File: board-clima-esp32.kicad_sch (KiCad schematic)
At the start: 54 parts, among them IC1 ESP32-S3-WROOM-1-N4, J1 Conn_01x06_Pin, J2 Screw_Terminal_01x03, J3 Conn_01x04_Pin, J5 Conn_01x05_Pin, J6 USB_C_Receptacle, Q1 AO3400A, Q2 AO3401A, Q3 AO3400A, SW1 RESET, SW2 BOOT, U1 AMS1117-3.3, U3 PC817, U4 PC817

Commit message: rev2 routing
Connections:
- net R_COM: now also U2.13 (CM2); no longer U2.4 (CM1)
- net R_NC: now also U2.11 (NC2); no longer U2.6 (NC1)
- net R_NO: now also U2.9 (NO2); no longer U2.8 (NO1)
- net at D1.2 (A), Q1.3 (D): now also U2.16 (S2); no longer U2.1 (S1)
- net at D2.1 (K), R8.2: now also U2.2 (R1); no longer U2.15 (R2)
- net at D1.1 (K), R4.2: now also U2.1 (S1); no longer U2.16 (S2)
- net at D2.2 (A), Q3.3 (D): now also U2.15 (R2); no longer U2.2 (R1)
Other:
- moved on the sheet: U2
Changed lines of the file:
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@@
   (junction (at 240.03 72.39) (diameter 0) (color 0 0 0 0)
   )
+  (junction (at 198.12 135.89) (diameter 0) (color 0 0 0 0)
+  )
+  (junction (at 102.87 26.67) (diameter 0) (color 0 0 0 0)
+  )
+  (junction (at 209.55 120.65) (diameter 0) (color 0 0 0 0)
+  )
+  (junction (at 300.99 78.74) (diameter 0) (color 0 0 0 0)
+  )
+  (junction (at 93.98 26.67) (diameter 0) (color 0 0 0 0)
+  )
+  (junction (at 240.03 69.85) (diameter 0) (color 0 0 0 0)
+  )
+  (junction (at 182.88 34.29) (diameter 0) (color 0 0 0 0)
+  )
+  (junction (at 182.88 85.09) (diameter 0) (color 0 0 0 0)
+  )
+  (junction (at 115.57 39.37) (diameter 0) (color 0 0 0 0)
+  )
+  (junction (at 186.69 99.06) (diameter 0) (color 0 0 0 0)
+  )
   (junction (at 92.71 152.4) (diameter 0) (color 0 0 0 0)
-  )
-  (junction (at 198.12 135.89) (diameter 0) (color 0 0 0 0)
-  )
-  (junction (at 102.87 26.67) (diameter 0) (color 0 0 0 0)
-  )
-  (junction (at 209.55 120.65) (diameter 0) (color 0 0 0 0)
-  )
-  (junction (at 300.99 78.74) (diameter 0) (color 0 0 0 0)
-  )
-  (junction (at 93.98 26.67) (diameter 0) (color 0 0 0 0)
-  )
-  (junction (at 240.03 69.85) (diameter 0) (color 0 0 0 0)
-  )
-  (junction (at 182.88 34.29) (diameter 0) (color 0 0 0 0)
-  )
-  (junction (at 182.88 85.09) (diameter 0) (color 0 0 0 0)
-  )
-  (junction (at 115.57 39.37) (diameter 0) (color 0 0 0 0)
-  )
-  (junction (at 186.69 99.06) (diameter 0) (color 0 0 0 0)
   )
   (junction (at 198.12 146.05) (diameter 0) (color 0 0 0 0)
@@
   (no_connect (at 240.03 52.07))
   (no_connect (at 45.72 64.77))
-  (no_connect (at 101.6 132.08))
   (no_connect (at 45.72 59.69))
   (no_connect (at 240.03 46.99))
@@
   (no_connect (at 45.72 57.15))
   (no_connect (at 207.01 44.45))
+  (no_connect (at 101.6 133.35))
   (no_connect (at 45.72 49.53))
   (no_connect (at 45.72 72.39))
@@
   (no_connect (at 45.72 82.55))
   (no_connect (at 240.03 34.29))
-  (no_connect (at 99.06 132.08))
   (no_connect (at 240.03 44.45))
   (no_connect (at 45.72 67.31))
@@
   (no_connect (at 45.72 74.93))
   (no_connect (at 207.01 67.31))
-  (no_connect (at 96.52 132.08))
+  (no_connect (at 99.06 133.35))
   (no_connect (at 207.01 49.53))
   (no_connect (at 207.01 54.61))
@@
   (no_connect (at 207.01 36.83))
   (no_connect (at 45.72 52.07))
+  (no_connect (at 96.52 133.35))
   (no_connect (at 207.01 57.15))
   (no_connect (at 240.03 36.83))
@@
     (stroke (width 0) (type default))
   )
+  (wire (pts (xy 92.71 148.59) (xy 92.71 152.4))
+    (stroke (width 0) (type default))
+  )
   (wire (pts (xy 397.51 77.47) (xy 403.86 77.47))
     (stroke (width 0) (type default))
@@
     (stroke (width 0) (type default))
   )
+  (wire (pts (xy 90.17 123.19) (xy 90.17 133.35))
+    (stroke (width 0) (type default))
+  )
   (wire (pts (xy 189.23 99.06) (xy 186.69 99.06))
     (stroke (width 0) (type default))
@@
     (stroke (width 0) (type default))
   )
-  (wire (pts (xy 90.17 147.32) (xy 90.17 149.86))
-    (stroke (width 0) (type default))
-  )
   (wire (pts (xy 45.72 24.13) (xy 53.34 24.13))
     (stroke (width 0) (type default))
@@
     (stroke (width 0) (type default))
   )
-  (wire (pts (xy 90.17 123.19) (xy 90.17 132.08))
-    (stroke (width 0) (type default))
-  )
   (wire (pts (xy 160.02 34.29) (xy 168.91 34.29))
     (stroke (width 0) (type default))
@@
     (stroke (width 0) (type default))
   )
+  (wire (pts (xy 92.71 128.27) (xy 92.71 133.35))
+    (stroke (width 0) (type default))
+  )
   (wire (pts (xy 300.99 73.66) (xy 300.99 78.74))
     (stroke (width 0) (type default))
@@
     (stroke (width 0) (type default))
   )
-  (wire (pts (xy 96.52 147.32) (xy 96.52 154.94))
-    (stroke (width 0) (type default))
-  )
   (wire (pts (xy 195.58 59.69) (xy 207.01 59.69))
     (stroke (width 0) (type default))
@@
     (stroke (width 0) (type default))
   )
+  (wire (pts (xy 99.06 148.59) (xy 99.06 152.4))
+    (stroke (width 0) (type default))
+  )
   (wire (pts (xy 209.55 128.27) (xy 209.55 130.81))
     (stroke (width 0) (type default))
@@
     (stroke (width 0) (type default))
   )
-  (wire (pts (xy 92.71 147.32) (xy 92.71 152.4))
-    (stroke (width 0) (type default))
-  )
   (wire (pts (xy 102.87 36.83) (xy 102.87 39.37))
     (stroke (width 0) (type default))
@@
     (stroke (width 0) (type default))
   )
+  (wire (pts (xy 96.52 148.59) (xy 96.52 154.94))
+    (stroke (width 0) (type default))
+  )
   (wire (pts (xy 173.99 128.27) (xy 173.99 130.81))
     (stroke (width 0) (type default))
@@
     (stroke (width 0) (type default))
   )
-  (wire (pts (xy 99.06 147.32) (xy 99.06 152.4))
-    (stroke (width 0) (type default))
-  )
   (wire (pts (xy 128.27 26.67) (xy 134.62 26.67))
     (stroke (width 0) (type default))
@@
     (stroke (width 0) (type default))
   )
+  (wire (pts (xy 90.17 148.59) (xy 90.17 149.86))
+    (stroke (width 0) (type default))
+  )
   (wire (pts (xy 166.37 140.97) (xy 173.99 140.97))
     (stroke (width 0) (type default))
   )
-  (wire (pts (xy 101.6 147.32) (xy 101.6 149.86))
-    (stroke (width 0) (type default))
-  )
   (wire (pts (xy 96.52 154.94) (xy 107.95 154.94))
     (stroke (width 0) (type default))
   )
+  (wire (pts (xy 101.6 148.59) (xy 101.6 149.86))
+    (stroke (width 0) (type default))
+  )
   (wire (pts (xy 198.12 133.35) (xy 198.12 135.89))
     (stroke (width 0) (type default))
@@
   )
   (wire (pts (xy 299.72 76.2) (xy 302.26 76.2))
-    (stroke (width 0) (type default))
-  )
-  (wire (pts (xy 92.71 128.27) (xy 92.71 132.08))
     (stroke (width 0) (type default))
   )
@@
     )
   )
-  (symbol (lib_id "HFD2:HFD2/00X-M-L2") (at 88.9 134.62 0) (unit 1)
-    (in_bom yes) (on_board yes) (dnp no) (fields_autoplaced)
-    (property "Reference" "U2" (at 104.14 139.7 0)
+  (symbol (lib_id "HFD2:HFD2/00X-M-L2") (at 88.9 146.05 0) (mirror x) (unit 1)
+    (in_bom yes) (on_board yes) (dnp no)
+    (property "Reference" "U2" (at 104.14 140.97 0)
       (effects (font (size 1.27 1.27)) (justify left))
     )
-    (property "Value" "~" (at 88.9 134.62 0)
+    (property "Value" "~" (at 88.9 146.05 0)
       (effects (font (size 1.27 1.27)))
     )
-    (property "Footprint" "HFD2:HFD2-00X-M-L2" (at 96.52 120.65 0)
-      (effects (font (size 1.27 1.27)) hide)
-    )
-    (property "Datasheet" "https://pdf1.alldatasheet.com/datasheet-pdf/download/660910/HONGFA/HFD2SLASH005-S-L2-D.html" (at 93.98 123.19 0)
-      (effects (font (size 1.27 1.27)) hide)
-    )
+    (property "Footprint" "HFD2:HFD2-00X-M-L2" (at 96.52 160.02 0)
+      (effects (font (size 1.27 1.27)) hide)
+    )
+    (property "Datasheet" "https://pdf1.alldatasheet.com/datasheet-pdf/download/660910/HONGFA/HFD2SLASH005-S-L2-D.html" (at 93.98 157.48 0)
+      (effects (font (size 1.27 1.27)) hide)
+    )

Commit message: silkscreen
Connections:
- net GND: now also J5.4 (Pin_4); no longer J5.1 (Pin_1)
- net GPIO3: now also J5.1 (Pin_1); no longer J5.4 (Pin_4)
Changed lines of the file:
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@@
+    (effects (font (size 1.27 1.27)) (justify left bottom))
+  )
+  (label "GPIO3" (at 374.65 36.83 0) (fields_autoplaced)
     (effects (font (size 1.27 1.27)) (justify left bottom))
   )
@@
     (effects (font (size 1.27 1.27)) (justify left bottom))
   )
+  (label "GPIO1" (at 374.65 31.75 0) (fields_autoplaced)
+    (effects (font (size 1.27 1.27)) (justify left bottom))
+  )
   (label "SCK" (at 173.99 85.09 0) (fields_autoplaced)
     (effects (font (size 1.27 1.27)) (justify left bottom))
@@
     (effects (font (size 1.27 1.27)) (justify left bottom))
   )
+  (label "GPIO2" (at 374.65 34.29 0) (fields_autoplaced)
+    (effects (font (size 1.27 1.27)) (justify left bottom))
+  )
   (label "R_NO" (at 386.08 59.69 0) (fields_autoplaced)
     (effects (font (size 1.27 1.27)) (justify left bottom))
@@
     (effects (font (size 1.27 1.27)) (justify left bottom))
   )
-  (label "GPIO1" (at 374.65 31.75 0) (fields_autoplaced)
-    (effects (font (size 1.27 1.27)) (justify left bottom))
-  )
   (label "BOILER_1" (at 33.02 158.75 0) (fields_autoplaced)
     (effects (font (size 1.27 1.27)) (justify left bottom))
@@
     (effects (font (size 1.27 1.27)) (justify left bottom))
   )
-  (label "GPIO3" (at 374.65 29.21 0) (fields_autoplaced)
-    (effects (font (size 1.27 1.27)) (justify left bottom))
-  )
   (label "R_NO" (at 175.26 130.81 0) (fields_autoplaced)
     (effects (font (size 1.27 1.27)) (justify left bottom))
@@
     (effects (font (size 1.27 1.27)) (justify left bottom))
   )
-  (label "GPIO2" (at 374.65 34.29 0) (fields_autoplaced)
-    (effects (font (size 1.27 1.27)) (justify left bottom))
-  )
   (label "BOILER_1" (at 173.99 72.39 0) (fields_autoplaced)
     (effects (font (size 1.27 1.27)) (justify left bottom))
@@
   (label "BOOT" (at 245.745 31.75 0) (fields_autoplaced)
     (effects (font (size 1.27 1.27)) (justify left bottom))
-  )
-  (symbol (lib_id "power:GND") (at 374.65 36.83 0) (unit 1)
-    (in_bom yes) (on_board yes) (dnp no) (fields_autoplaced)
-    (property "Reference" "#PWR034" (at 374.65 43.18 0)
-      (effects (font (size 1.27 1.27)) hide)
-    )
-    (property "Value" "GND" (at 374.65 41.91 0)
-      (effects (font (size 1.27 1.27)))
-    )
-    (property "Footprint" "" (at 374.65 36.83 0)
-      (effects (font (size 1.27 1.27)) hide)
-    )
-    (property "Datasheet" "" (at 374.65 36.83 0)
-      (effects (font (size 1.27 1.27)) hide)
-    )
-    (pin "1")
-    (instances
-      (project "board-clima-esp32"
-        (path "/ec184202-d4fa-4f1f-9fe7-c32d14dd4c20"
-          (reference "#PWR034") (unit 1)
-        )
-      )
-    )
   )
   (symbol (lib_id "power:+3.3V") (at 335.28 26.67 0) (unit 1)
@@
         )
       )
+    )
+  )
+  (symbol (lib_id "power:GND") (at 374.65 29.21 270) (unit 1)
+    (in_bom yes) (on_board yes) (dnp no) (fields_autoplaced)
+    (property "Reference" "#PWR021" (at 368.3 29.21 0)
+      (effects (font (size 1.27 1.27)) hide)
+    )
+    (property "Value" "GND" (at 370.84 29.21 90)
+      (effects (font (size 1.27 1.27)) (justify right))
+    )
+    (property "Footprint" "" (at 374.65 29.21 0)
+      (effects (font (size 1.27 1.27)) hide)
+    )
+    (property "Datasheet" "" (at 374.65 29.21 0)
+      (effects (font (size 1.27 1.27)) hide)
+    )
+    (pin "1")
+    (instances
+      (project "board-clima-esp32"
+        (path "/ec184202-d4fa-4f1f-9fe7-c32d14dd4c20"
+          (reference "#PWR021") (unit 1)
+        )
+      )

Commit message: drc passes
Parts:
- added D11: LED, LED_SMD:LED_0805_2012Metric, symbol Device:LED
- added R18: 220, Resistor_SMD:R_0805_2012Metric, symbol Device:R
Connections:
- net GND: now also R18.2
- net GPIO3: now also D11.2 (A)
- new net: D11.1 (K), R18.1
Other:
- note added: "USER LED"

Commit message: silkscreen
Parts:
- D10, D8, D9: footprint Diode_SMD:D_SOD-323 -> Diode_SMD:D_SOD-123
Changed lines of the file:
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@@
       (effects (font (size 1.27 1.27)) (justify left))
     )
-    (property "Footprint" "Diode_SMD:D_SOD-323" (at 222.25 134.62 0)
+    (property "Footprint" "Diode_SMD:D_SOD-123" (at 222.25 134.62 0)
       (effects (font (size 1.27 1.27)) hide)
     )
@@
       (effects (font (size 1.27 1.27)) (justify left))
     )
-    (property "Footprint" "Diode_SMD:D_SOD-323" (at 209.55 134.62 0)
+    (property "Footprint" "Diode_SMD:D_SOD-123" (at 209.55 134.62 0)
       (effects (font (size 1.27 1.27)) hide)
     )
@@
       (effects (font (size 1.27 1.27)) (justify left))
     )
-    (property "Footprint" "Diode_SMD:D_SOD-323" (at 193.04 144.78 0)
-      (effects (font (size 1.27 1.27)) hide)
-    )
+    (property "Footprint" "Diode_SMD:D_SOD-123" (at 193.04 144.78 0)
+      (effects (font (size 1.27 1.27)) hide)
+    )

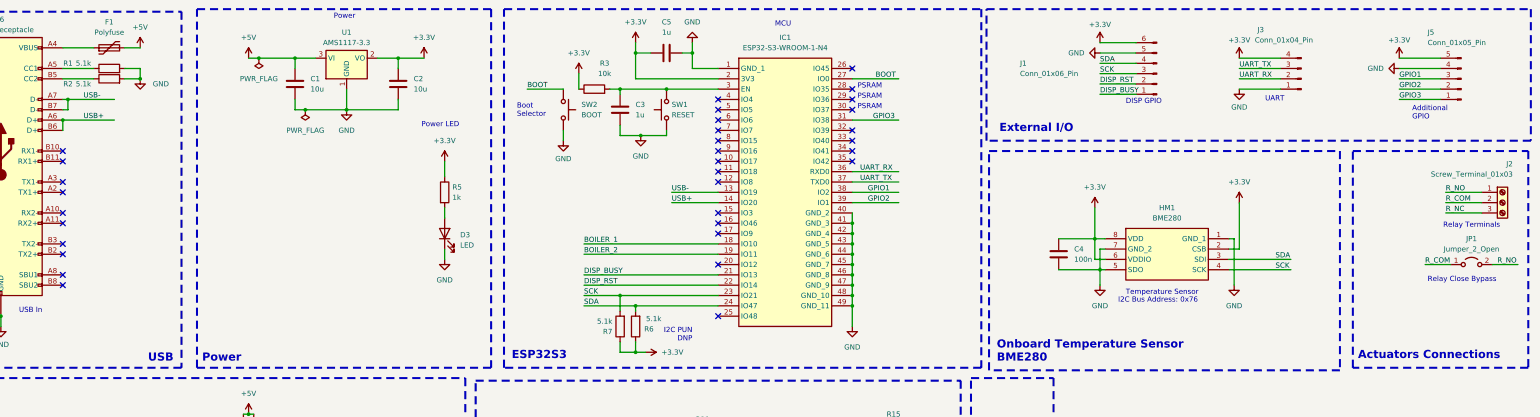
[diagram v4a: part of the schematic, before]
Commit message: new PWR connector, front copper pour
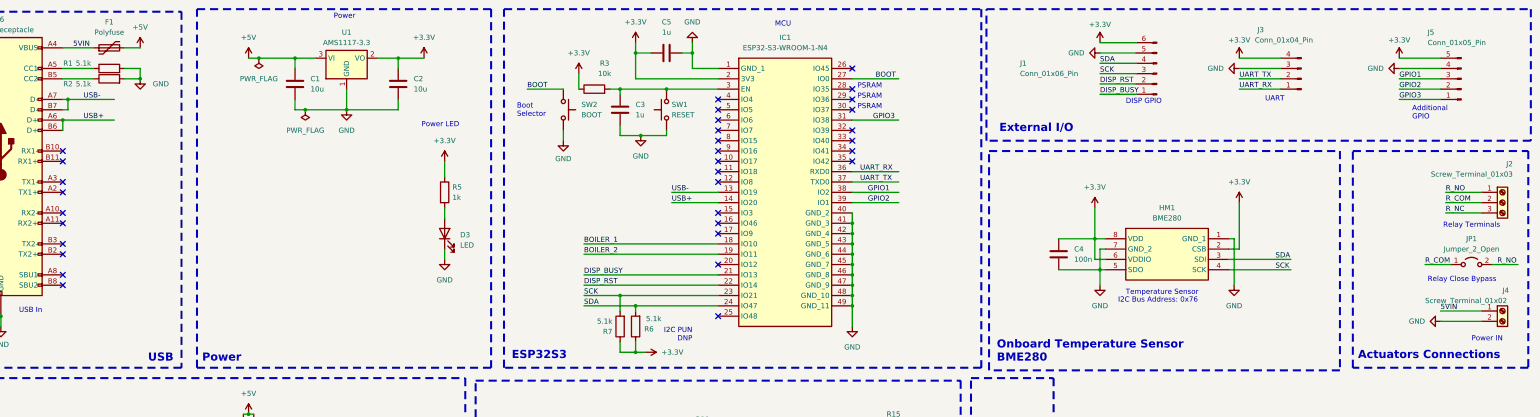
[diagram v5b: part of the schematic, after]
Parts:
- added J4: Screw_Terminal_01x02, XYEK500-5.08-3P:XYEK500-5.08-2P, symbol Connector:Screw_Terminal_01x02
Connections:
- net GND: now also J3.3 (Pin_3), J4.2 (Pin_2); no longer J3.1 (Pin_1)
- net UART_RX: now also J3.1 (Pin_1); no longer J3.2 (Pin_2)
- net UART_TX: now also J3.2 (Pin_2); no longer J3.3 (Pin_3)
- net 5VIN: now reaches F1.1, J6.A4 (VBUS), J6.A9 (VBUS), J6.B4 (VBUS), J6.B9 (VBUS)
- net 5VIN: now also J4.1 (Pin_1)
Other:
- note added: "Power IN"
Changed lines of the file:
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@@
+    (stroke (width 0) (type default))
+  )
+  (wire (pts (xy 384.81 91.44) (xy 394.97 91.44))
     (stroke (width 0) (type default))
   )
@@
   )
   (wire (pts (xy 245.11 146.05) (xy 248.92 146.05))
+    (stroke (width 0) (type default))
+  )
+  (wire (pts (xy 384.81 88.9) (xy 394.97 88.9))
     (stroke (width 0) (type default))
   )
@@
     (effects (font (size 1.27 1.27) (color 255 0 0 1)) (justify left bottom))
   )
+  (text "Power IN" (at 392.43 96.52 0)
+    (effects (font (size 1.27 1.27)) (justify left bottom))
+  )
   (text "UART" (at 341.63 37.465 0)
     (effects (font (size 1.27 1.27)) (justify left bottom))
@@
     (effects (font (size 1.27 1.27)) (justify left bottom))
   )
+  (label "5VIN" (at 48.26 24.13 0) (fields_autoplaced)
+    (effects (font (size 1.27 1.27)) (justify left bottom))
+  )
   (label "GPIO1" (at 374.65 31.75 0) (fields_autoplaced)
     (effects (font (size 1.27 1.27)) (justify left bottom))
@@
     (effects (font (size 1.27 1.27)) (justify left bottom))
   )
-  (label "UART_TX" (at 335.28 29.21 0) (fields_autoplaced)
+  (label "UART_TX" (at 335.28 31.75 0) (fields_autoplaced)
     (effects (font (size 1.27 1.27)) (justify left bottom))
   )
@@
     (effects (font (size 1.27 1.27)) (justify left bottom))
   )
-  (label "UART_RX" (at 335.28 31.75 0) (fields_autoplaced)
+  (label "UART_RX" (at 335.28 34.29 0) (fields_autoplaced)
     (effects (font (size 1.27 1.27)) (justify left bottom))
   )
@@
   )
   (label "R_NO" (at 398.78 77.47 0) (fields_autoplaced)
+    (effects (font (size 1.27 1.27)) (justify left bottom))
+  )
+  (label "5VIN" (at 384.81 88.9 0) (fields_autoplaced)
     (effects (font (size 1.27 1.27)) (justify left bottom))
   )
@@
     )
   )
-  (symbol (lib_id "power:GND") (at 335.28 34.29 0) (unit 1)
-    (in_bom yes) (on_board yes) (dnp no) (fields_autoplaced)
-    (property "Reference" "#PWR019" (at 335.28 40.64 0)
-      (effects (font (size 1.27 1.27)) hide)
-    )
-    (property "Value" "GND" (at 335.28 38.735 0)
-      (effects (font (size 1.27 1.27)))
-    )
-    (property "Footprint" "" (at 335.28 34.29 0)
-      (effects (font (size 1.27 1.27)) hide)
-    )
-    (property "Datasheet" "" (at 335.28 34.29 0)
-      (effects (font (size 1.27 1.27)) hide)
-    )
-    (pin "1")
-    (instances
-      (project "board-clima-esp32"
-        (path "/ec184202-d4fa-4f1f-9fe7-c32d14dd4c20"
-          (reference "#PWR019") (unit 1)
+  (symbol (lib_id "power:GND") (at 384.81 91.44 270) (unit 1)
+    (in_bom yes) (on_board yes) (dnp no) (fields_autoplaced)
+    (property "Reference" "#PWR035" (at 378.46 91.44 0)
+      (effects (font (size 1.27 1.27)) hide)
+    )
+    (property "Value" "GND" (at 381 91.44 90)
+      (effects (font (size 1.27 1.27)) (justify right))
+    )
+    (property "Footprint" "" (at 384.81 91.44 0)
+      (effects (font (size 1.27 1.27)) hide)
+    )
+    (property "Datasheet" "" (at 384.81 91.44 0)
+      (effects (font (size 1.27 1.27)) hide)
+    )
+    (pin "1")
+    (instances
+      (project "board-clima-esp32"
+        (path "/ec184202-d4fa-4f1f-9fe7-c32d14dd4c20"
+          (reference "#PWR035") (unit 1)
         )
       )
@@
     )
   )
+  (symbol (lib_id "power:GND") (at 335.28 29.21 270) (unit 1)
+    (in_bom yes) (on_board yes) (dnp no) (fields_autoplaced)
+    (property "Reference" "#PWR036" (at 328.93 29.21 0)
+      (effects (font (size 1.27 1.27)) hide)
+    )
+    (property "Value" "GND" (at 331.47 29.21 90)
+      (effects (font (size 1.27 1.27)) (justify right))
+    )
+    (property "Footprint" "" (at 335.28 29.21 0)
+      (effects (font (size 1.27 1.27)) hide)
+    )
+    (property "Datasheet" "" (at 335.28 29.21 0)
+      (effects (font (size 1.27 1.27)) hide)
+    )
+    (pin "1")
+    (instances
+      (project "board-clima-esp32"
+        (path "/ec184202-d4fa-4f1f-9fe7-c32d14dd4c20"
+          (reference "#PWR036") (unit 1)
+        )
+      )
+    )
+  )
   (symbol (lib_id "Device:R") (at 182.88 92.71 180) (unit 1)
     (in_bom yes) (on_board yes) (dnp no) (fields_autoplaced)
@@
         )
       )
+    )
+  )
+  (symbol (lib_id "Connector:Screw_Terminal_01x02") (at 400.05 88.9 0) (unit 1)
+    (in_bom yes) (on_board yes) (dnp no)
+    (property "Reference" "J4" (at 400.05 83.82 0)
+      (effects (font (size 1.27 1.27)) (justify left))
+    )
+    (property "Value" "Screw_Terminal_01x02" (at 381 86.36 0)
+      (effects (font (size 1.27 1.27)) (justify left))
+    )
+    (property "Footprint" "XYEK500-5.08-3P:XYEK500-5.08-2P" (at 400.05 88.9 0)
+      (effects (font (size 1.27 1.27)) hide)
+    )
+    (property "Datasheet" "~" (at 400.05 88.9 0)
+      (effects (font (size 1.27 1.27)) hide)
+    )
+    (pin "2")
+    (pin "1")
+    (instances
+      (project "board-clima-esp32"
+        (path "/ec184202-d4fa-4f1f-9fe7-c32d14dd4c20"
+          (reference "J4") (unit 1)
+        )
+      )
